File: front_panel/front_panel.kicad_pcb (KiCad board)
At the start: 2 copper layers, 103 x 30.5 mm, 1 part

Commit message: t add pmos boaard
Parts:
- added J1: Conn_Coaxial, 0my_footprints:sma_panel, F.Cu at (182.6, 103.9)
- added J2: Conn_Coaxial, 0my_footprints:sma_panel, F.Cu at (172.6, 118.7)
- added J3: Conn_Coaxial, 0my_footprints:sma_panel, F.Cu at (162.6, 103.9)
- added J4: Conn_Coaxial, 0my_footprints:sma_panel, F.Cu at (152.6, 118.7)
- added J5: Conn_Coaxial, 0my_footprints:sma_panel, F.Cu at (142.6, 103.9)
- added J6: Conn_Coaxial, 0my_footprints:sma_panel, F.Cu at (112.6, 118.7)
- added J7: Conn_Coaxial, 0my_footprints:sma_panel, F.Cu at (122.6, 103.9)
- added J8: Conn_Coaxial, 0my_footprints:sma_panel, F.Cu at (132.6, 118.7)
- H1: footprint TestPoint:TestPoint_Pad_1.0x1.0mm -> MountingHole:MountingHole_3.2mm_M3_Pad_Via
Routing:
- net GND: vias 12 -> 4
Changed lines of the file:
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@@
     (thickness 1.6)
     (drawings 8)
-    (tracks 13)
+    (tracks 5)
     (zones 0)
-    (modules 1)
+    (modules 9)
     (nets 2)
   )
@@
     (mod_text_size 1 1)
     (mod_text_width 0.15)
-    (pad_size 1.524 1.524)
-    (pad_drill 0.762)
+    (pad_size 13 13)
+    (pad_drill 6.5)
     (pad_to_mask_clearance 0.051)
     (solder_mask_min_width 0.25)
@@
       (drillshape 0)
       (scaleselection 1)
-      (outputdirectory "gerbers/front/"))
+      (outputdirectory "gerbers/front_v2/"))
   )
   (net 0 "")
@@
     (add_net GND)
   )
-  (module TestPoint:TestPoint_Pad_1.0x1.0mm (layer F.Cu)
+  (module 0my_footprints:sma_panel (layer F.Cu)
+    (at 132.565 118.715)
+    (fp_text reference J8 (at 0 0.5) (layer F.SilkS)
+      (effects (font (size 1 1) (thickness 0.15)))
+    )
+    (fp_text value Conn_Coaxial (at 0 -0.5) (layer F.Fab)
+      (effects (font (size 1 1) (thickness 0.15)))
+    )
+    (pad 2 thru_hole circle (at 0 0) (size 13 13) (drill 7.5) (layers *.Cu *.Mask)
+      (net 1 GND))
+  )
+  (module 0my_footprints:sma_panel (layer F.Cu)
+    (at 122.565 103.915)
+    (fp_text reference J7 (at 0 0.5) (layer F.SilkS)
+      (effects (font (size 1 1) (thickness 0.15)))
+    )
+    (fp_text value Conn_Coaxial (at 0 -0.5) (layer F.Fab)
+      (effects (font (size 1 1) (thickness 0.15)))
+    )
+    (pad 2 thru_hole circle (at 0 0) (size 13 13) (drill 7.5) (layers *.Cu *.Mask)
+      (net 1 GND))
+  )
+  (module 0my_footprints:sma_panel (layer F.Cu)
+    (at 112.565 118.715)
+    (fp_text reference J6 (at 0 0.5) (layer F.SilkS)
+      (effects (font (size 1 1) (thickness 0.15)))
+    )
+    (fp_text value Conn_Coaxial (at 0 -0.5) (layer F.Fab)
+      (effects (font (size 1 1) (thickness 0.15)))
+    )
+    (pad 2 thru_hole circle (at 0 0) (size 13 13) (drill 7.5) (layers *.Cu *.Mask)
+      (net 1 GND))
+  )
+  (module 0my_footprints:sma_panel (layer F.Cu)
+    (at 142.565 103.915)
+    (fp_text reference J5 (at 0 0.5) (layer F.SilkS)
+      (effects (font (size 1 1) (thickness 0.15)))
+    )
+    (fp_text value Conn_Coaxial (at 0 -0.5) (layer F.Fab)
+      (effects (font (size 1 1) (thickness 0.15)))
+    )
+    (pad 2 thru_hole circle (at 0 0) (size 13 13) (drill 7.5) (layers *.Cu *.Mask)
+      (net 1 GND))
+  )
+  (module 0my_footprints:sma_panel (layer F.Cu)
+    (at 172.565 118.715)
+    (fp_text reference J2 (at 0 0.5) (layer F.SilkS)
+      (effects (font (size 1 1) (thickness 0.15)))
+    )
+    (fp_text value Conn_Coaxial (at 0 -0.5) (layer F.Fab)
+      (effects (font (size 1 1) (thickness 0.15)))
+    )
+    (pad 2 thru_hole circle (at 0 0) (size 13 13) (drill 7.5) (layers *.Cu *.Mask)
+      (net 1 GND))
+  )
+  (module 0my_footprints:sma_panel (layer F.Cu)
+    (at 152.565 118.715)
+    (fp_text reference J4 (at 0 0.5) (layer F.SilkS)
+      (effects (font (size 1 1) (thickness 0.15)))
+    )
+    (fp_text value Conn_Coaxial (at 0 -0.5) (layer F.Fab)
+      (effects (font (size 1 1) (thickness 0.15)))
+    )
+    (pad 2 thru_hole circle (at 0 0) (size 13 13) (drill 7.5) (layers *.Cu *.Mask)
+      (net 1 GND))
+  )
+  (module 0my_footprints:sma_panel (layer F.Cu)
+    (at 162.565 103.915)
+    (fp_text reference J3 (at 0 0.5) (layer F.SilkS)
+      (effects (font (size 1 1) (thickness 0.15)))
+    )
+    (fp_text value Conn_Coaxial (at 0 -0.5) (layer F.Fab)
+      (effects (font (size 1 1) (thickness 0.15)))
+    )
+    (pad 2 thru_hole circle (at 0 0) (size 13 13) (drill 7.5) (layers *.Cu *.Mask)
+      (net 1 GND))
+  )
+  (module 0my_footprints:sma_panel (layer F.Cu)
+    (at 182.565 103.915)
+    (fp_text reference J1 (at 0 0.5) (layer F.SilkS)
+      (effects (font (size 1 1) (thickness 0.15)))
+    )
+    (fp_text value Conn_Coaxial (at 0 -0.5) (layer F.Fab)
+      (effects (font (size 1 1) (thickness 0.15)))
+    )
+    (pad 2 thru_hole circle (at 0 0) (size 13 13) (drill 7.5) (layers *.Cu *.Mask)
+      (net 1 GND))
+  )
+  (module MountingHole:MountingHole_3.2mm_M3_Pad_Via (layer F.Cu)
     (at 195 110)
-    (descr "SMD rectangular pad as test Point, square 1.0mm side length")
-    (tags "test point SMD pad rectangle square")
+    (descr "Mounting Hole 3.2mm, M3")
+    (tags "mounting hole 3.2mm m3")
     (attr virtual)
     (fp_text reference H1 (at 0 -4.2) (layer F.SilkS)
@@
       (effects (font (size 1 1) (thickness 0.15)))
     )
-    (fp_line (start 1 1) (end -1 1) (layer F.CrtYd) (width 0.05))
-    (fp_line (start 1 1) (end 1 -1) (layer F.CrtYd) (width 0.05))
-    (fp_line (start -1 -1) (end -1 1) (layer F.CrtYd) (width 0.05))
-    (fp_line (start -1 -1) (end 1 -1) (layer F.CrtYd) (width 0.05))
-    (fp_line (start -0.7 0.7) (end -0.7 -0.7) (layer F.SilkS) (width 0.12))
-    (fp_line (start 0.7 0.7) (end -0.7 0.7) (layer F.SilkS) (width 0.12))
-    (fp_line (start 0.7 -0.7) (end 0.7 0.7) (layer F.SilkS) (width 0.12))
-    (fp_line (start -0.7 -0.7) (end 0.7 -0.7) (layer F.SilkS) (width 0.12))
+    (fp_circle (center 0 0) (end 3.45 0) (layer F.CrtYd) (width 0.05))
+    (fp_circle (center 0 0) (end 3.2 0) (layer Cmts.User) (width 0.15))
     (fp_text user %R (at 0.3 0) (layer F.Fab)
       (effects (font (size 1 1) (thickness 0.15)))
     )
-    (pad 1 smd rect (at 0 0) (size 1 1) (layers F.Cu F.Mask)
+    (pad 1 thru_hole circle (at 1.697056 -1.697056) (size 0.8 0.8) (drill 0.5) (layers *.Cu *.Mask)
+      (net 1 GND))
+    (pad 1 thru_hole circle (at 0 -2.4) (size 0.8 0.8) (drill 0.5) (layers *.Cu *.Mask)
+      (net 1 GND))
+    (pad 1 thru_hole circle (at -1.697056 -1.697056) (size 0.8 0.8) (drill 0.5) (layers *.Cu *.Mask)
+      (net 1 GND))
+    (pad 1 thru_hole circle (at -2.4 0) (size 0.8 0.8) (drill 0.5) (layers *.Cu *.Mask)
+      (net 1 GND))
+    (pad 1 thru_hole circle (at -1.697056 1.697056) (size 0.8 0.8) (drill 0.5) (layers *.Cu *.Mask)
+      (net 1 GND))
+    (pad 1 thru_hole circle (at 0 2.4) (size 0.8 0.8) (drill 0.5) (layers *.Cu *.Mask)
+      (net 1 GND))
+    (pad 1 thru_hole circle (at 1.697056 1.697056) (size 0.8 0.8) (drill 0.5) (layers *.Cu *.Mask)
+      (net 1 GND))
+    (pad 1 thru_hole circle (at 2.4 0) (size 0.8 0.8) (drill 0.5) (layers *.Cu *.Mask)
+      (net 1 GND))
+    (pad 1 thru_hole circle (at 0 0) (size 6.4 6.4) (drill 3.2) (layers *.Cu *.Mask)
       (net 1 GND))
   )
@@
   (via (at 195.13 100) (size 5.8) (drill 3.5) (layers F.Cu B.Cu) (net 1))
   (via (at 195.13 122.63) (size 5.8) (drill 3.5) (layers F.Cu B.Cu) (net 1))
-  (via (at 112.565 118.715) (size 13) (drill 6.5) (layers F.Cu B.Cu) (net 1))
-  (via (at 132.565 118.715) (size 13) (drill 6.5) (layers F.Cu B.Cu) (net 1))
-  (via (at 152.565 118.715) (size 13) (drill 6.5) (layers F.Cu B.Cu) (net 1))
-  (via (at 172.565 118.715) (size 13) (drill 6.5) (layers F.Cu B.Cu) (net 1))
-  (via (at 122.565 103.915) (size 13) (drill 6.5) (layers F.Cu B.Cu) (net 1))
-  (via (at 142.565 103.915) (size 13) (drill 6.5) (layers F.Cu B.Cu) (net 1))
-  (via (at 162.565 103.915) (size 13) (drill 6.5) (layers F.Cu B.Cu) (net 1))
-  (via (at 182.565 103.915) (size 13) (drill 6.5) (layers F.Cu B.Cu) (net 1))
   (segment (start 152.565 118.715) (end 172.565 118.715) (width 0.25) (layer F.Cu) (net 1))
   (zone (net 1) (net_name GND) (layer F.Cu) (hatch edge 0.508)

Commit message: Update to pmosboard
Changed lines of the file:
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@@
       (effects (font (size 1 1) (thickness 0.15)))
     )
-    (pad 2 thru_hole circle (at 0 0) (size 13 13) (drill 7.5) (layers *.Cu *.Mask)
+    (pad 2 thru_hole circle (at 0 0) (size 13 13) (drill 9) (layers *.Cu *.Mask)
       (net 1 GND))
   )
@@
       (effects (font (size 1 1) (thickness 0.15)))
     )
-    (pad 2 thru_hole circle (at 0 0) (size 13 13) (drill 7.5) (layers *.Cu *.Mask)
+    (pad 2 thru_hole circle (at 0 0) (size 13 13) (drill 9) (layers *.Cu *.Mask)
       (net 1 GND))
   )
@@
       (effects (font (size 1 1) (thickness 0.15)))
     )
-    (pad 2 thru_hole circle (at 0 0) (size 13 13) (drill 7.5) (layers *.Cu *.Mask)
+    (pad 2 thru_hole circle (at 0 0) (size 13 13) (drill 9) (layers *.Cu *.Mask)
       (net 1 GND))
   )
@@
       (effects (font (size 1 1) (thickness 0.15)))
     )
-    (pad 2 thru_hole circle (at 0 0) (size 13 13) (drill 7.5) (layers *.Cu *.Mask)
+    (pad 2 thru_hole circle (at 0 0) (size 13 13) (drill 9) (layers *.Cu *.Mask)
       (net 1 GND))
   )
@@
       (effects (font (size 1 1) (thickness 0.15)))
     )
-    (pad 2 thru_hole circle (at 0 0) (size 13 13) (drill 7.5) (layers *.Cu *.Mask)
+    (pad 2 thru_hole circle (at 0 0) (size 13 13) (drill 9) (layers *.Cu *.Mask)
       (net 1 GND))
   )
@@
       (effects (font (size 1 1) (thickness 0.15)))
     )
-    (pad 2 thru_hole circle (at 0 0) (size 13 13) (drill 7.5) (layers *.Cu *.Mask)
+    (pad 2 thru_hole circle (at 0 0) (size 13 13) (drill 9) (layers *.Cu *.Mask)
       (net 1 GND))
   )
@@
       (effects (font (size 1 1) (thickness 0.15)))
     )
-    (pad 2 thru_hole circle (at 0 0) (size 13 13) (drill 7.5) (layers *.Cu *.Mask)
+    (pad 2 thru_hole circle (at 0 0) (size 13 13) (drill 9) (layers *.Cu *.Mask)
       (net 1 GND))
   )
@@
       (effects (font (size 1 1) (thickness 0.15)))
     )
-    (pad 2 thru_hole circle (at 0 0) (size 13 13) (drill 7.5) (layers *.Cu *.Mask)
+    (pad 2 thru_hole circle (at 0 0) (size 13 13) (drill 9) (layers *.Cu *.Mask)
       (net 1 GND))
   )

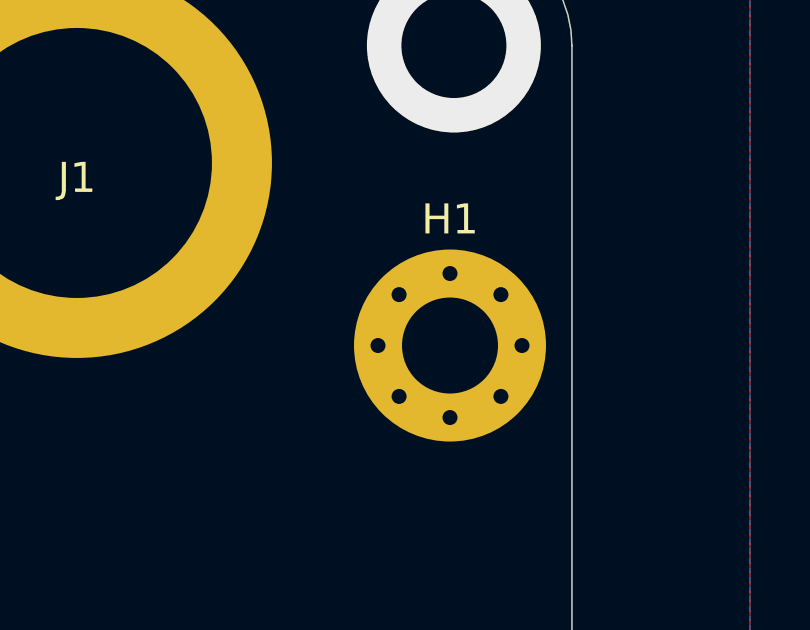
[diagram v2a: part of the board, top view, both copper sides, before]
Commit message: fix problem with front-panel... elminate thermals
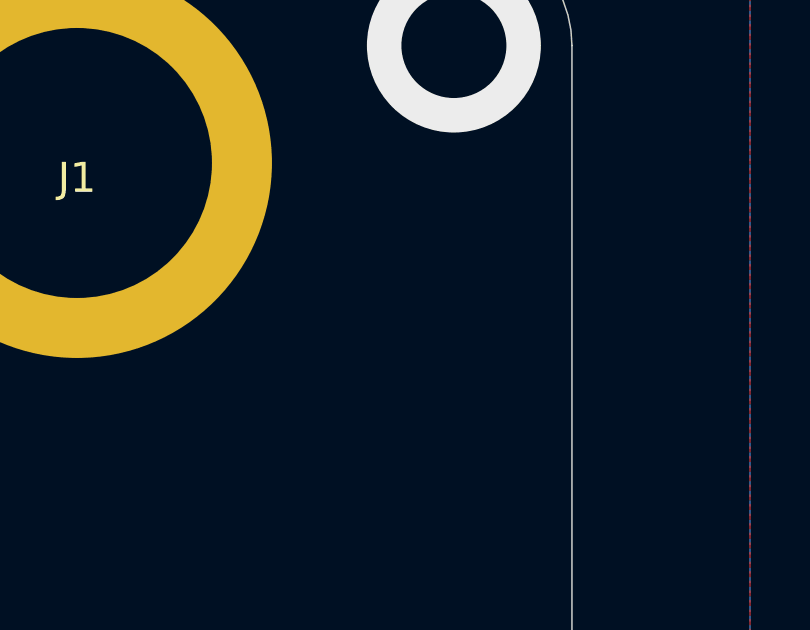
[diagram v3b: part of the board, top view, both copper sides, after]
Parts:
- removed H1: MountingHole, MountingHole:MountingHole_3.2mm_M3_Pad_Via
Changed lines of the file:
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@@
     (tracks 5)
     (zones 0)
-    (modules 9)
+    (modules 8)
     (nets 2)
   )
@@
       (drillshape 0)
       (scaleselection 1)
-      (outputdirectory "gerbers/front_v2/"))
+      (outputdirectory "gerbers/front_v3/"))
   )
   (net 0 "")
@@
     )
     (pad 2 thru_hole circle (at 0 0) (size 13 13) (drill 9) (layers *.Cu *.Mask)
-      (net 1 GND))
-  )
-  (module MountingHole:MountingHole_3.2mm_M3_Pad_Via (layer F.Cu)
-    (at 195 110)
-    (descr "Mounting Hole 3.2mm, M3")
-    (tags "mounting hole 3.2mm m3")
-    (attr virtual)
-    (fp_text reference H1 (at 0 -4.2) (layer F.SilkS)
-      (effects (font (size 1 1) (thickness 0.15)))
-    )
-    (fp_text value MountingHole (at 0 4.2) (layer F.Fab)
-      (effects (font (size 1 1) (thickness 0.15)))
-    )
-    (fp_circle (center 0 0) (end 3.45 0) (layer F.CrtYd) (width 0.05))
-    (fp_circle (center 0 0) (end 3.2 0) (layer Cmts.User) (width 0.15))
-    (fp_text user %R (at 0.3 0) (layer F.Fab)
-      (effects (font (size 1 1) (thickness 0.15)))
-    )
-    (pad 1 thru_hole circle (at 1.697056 -1.697056) (size 0.8 0.8) (drill 0.5) (layers *.Cu *.Mask)
-      (net 1 GND))
-    (pad 1 thru_hole circle (at 0 -2.4) (size 0.8 0.8) (drill 0.5) (layers *.Cu *.Mask)
-      (net 1 GND))
-    (pad 1 thru_hole circle (at -1.697056 -1.697056) (size 0.8 0.8) (drill 0.5) (layers *.Cu *.Mask)
-      (net 1 GND))
-    (pad 1 thru_hole circle (at -2.4 0) (size 0.8 0.8) (drill 0.5) (layers *.Cu *.Mask)
-      (net 1 GND))
-    (pad 1 thru_hole circle (at -1.697056 1.697056) (size 0.8 0.8) (drill 0.5) (layers *.Cu *.Mask)
-      (net 1 GND))
-    (pad 1 thru_hole circle (at 0 2.4) (size 0.8 0.8) (drill 0.5) (layers *.Cu *.Mask)
-      (net 1 GND))
-    (pad 1 thru_hole circle (at 1.697056 1.697056) (size 0.8 0.8) (drill 0.5) (layers *.Cu *.Mask)
-      (net 1 GND))
-    (pad 1 thru_hole circle (at 2.4 0) (size 0.8 0.8) (drill 0.5) (layers *.Cu *.Mask)
-      (net 1 GND))
-    (pad 1 thru_hole circle (at 0 0) (size 6.4 6.4) (drill 3.2) (layers *.Cu *.Mask)
       (net 1 GND))
   )
@@
   (segment (start 152.565 118.715) (end 172.565 118.715) (width 0.25) (layer F.Cu) (net 1))
   (zone (net 1) (net_name GND) (layer F.Cu) (hatch edge 0.508)
-    (connect_pads (clearance 0.508))
+    (connect_pads yes (clearance 0.508))
     (min_thickness 0.254)
     (fill yes (arc_segments 32) (thermal_gap 0.508) (thermal_bridge_width 0.508))
